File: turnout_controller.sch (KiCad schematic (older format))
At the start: 25 parts, among them J1 DCC Input, J2 Conn_01x04, J3 Servo Motor, J4 LED Connect, SW1 SW_Push, SW2 SW_Push, U1 AP65111A, U2 MKE04P24M48SF0

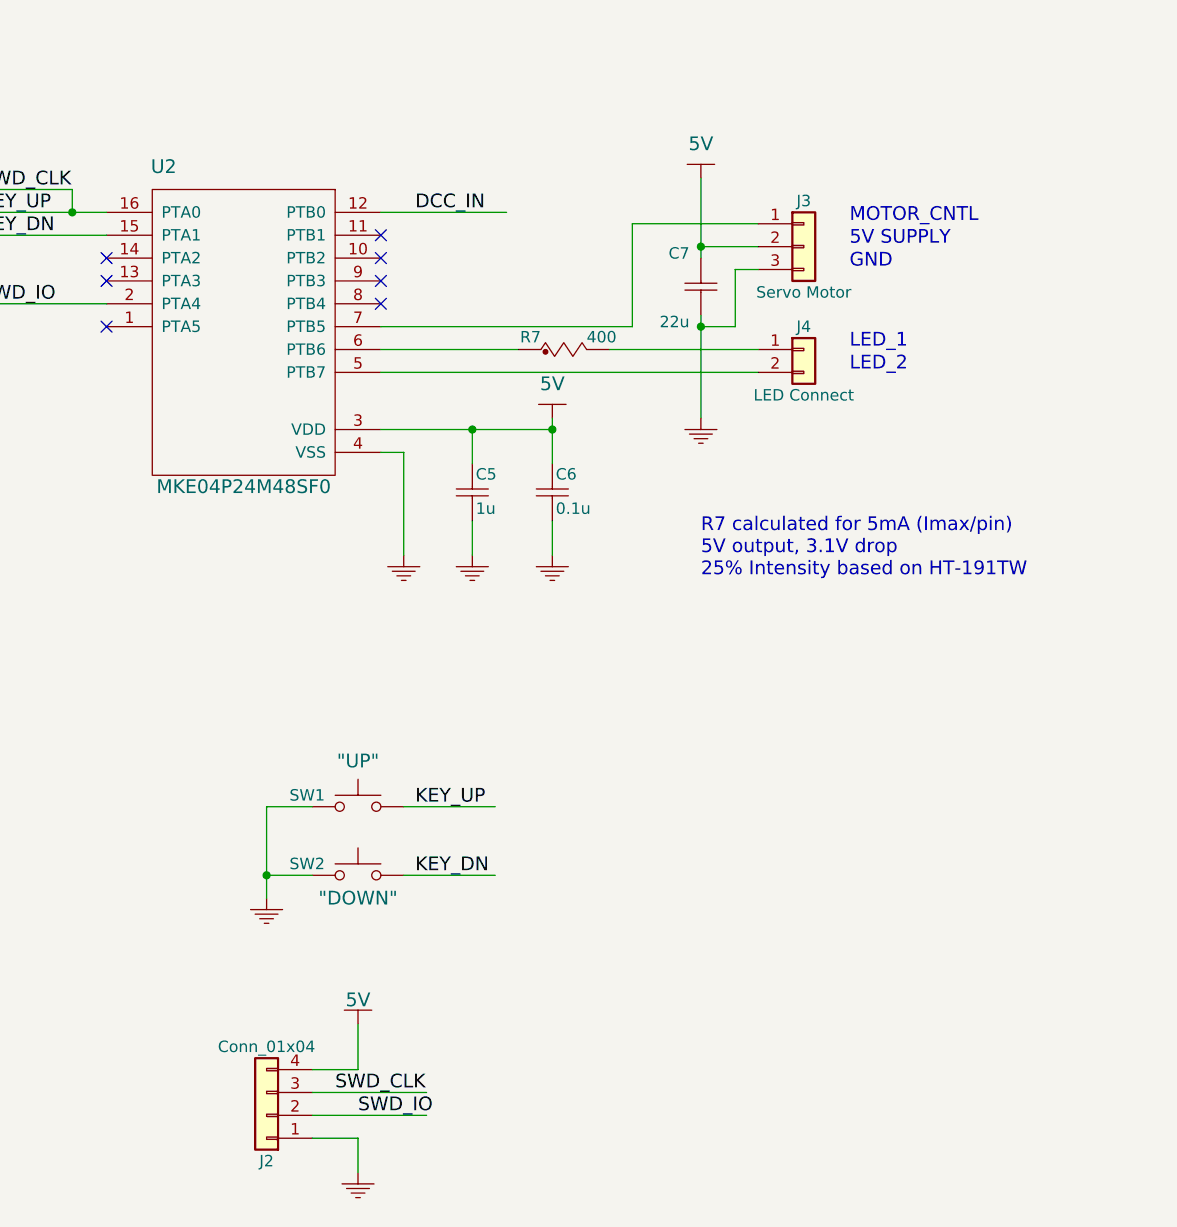
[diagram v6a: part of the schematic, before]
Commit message: 1. New PCB layout based around new positioning of buttons.
2. Optimizing distance between buck circuit components.

3. Added optional on-board LEDs.
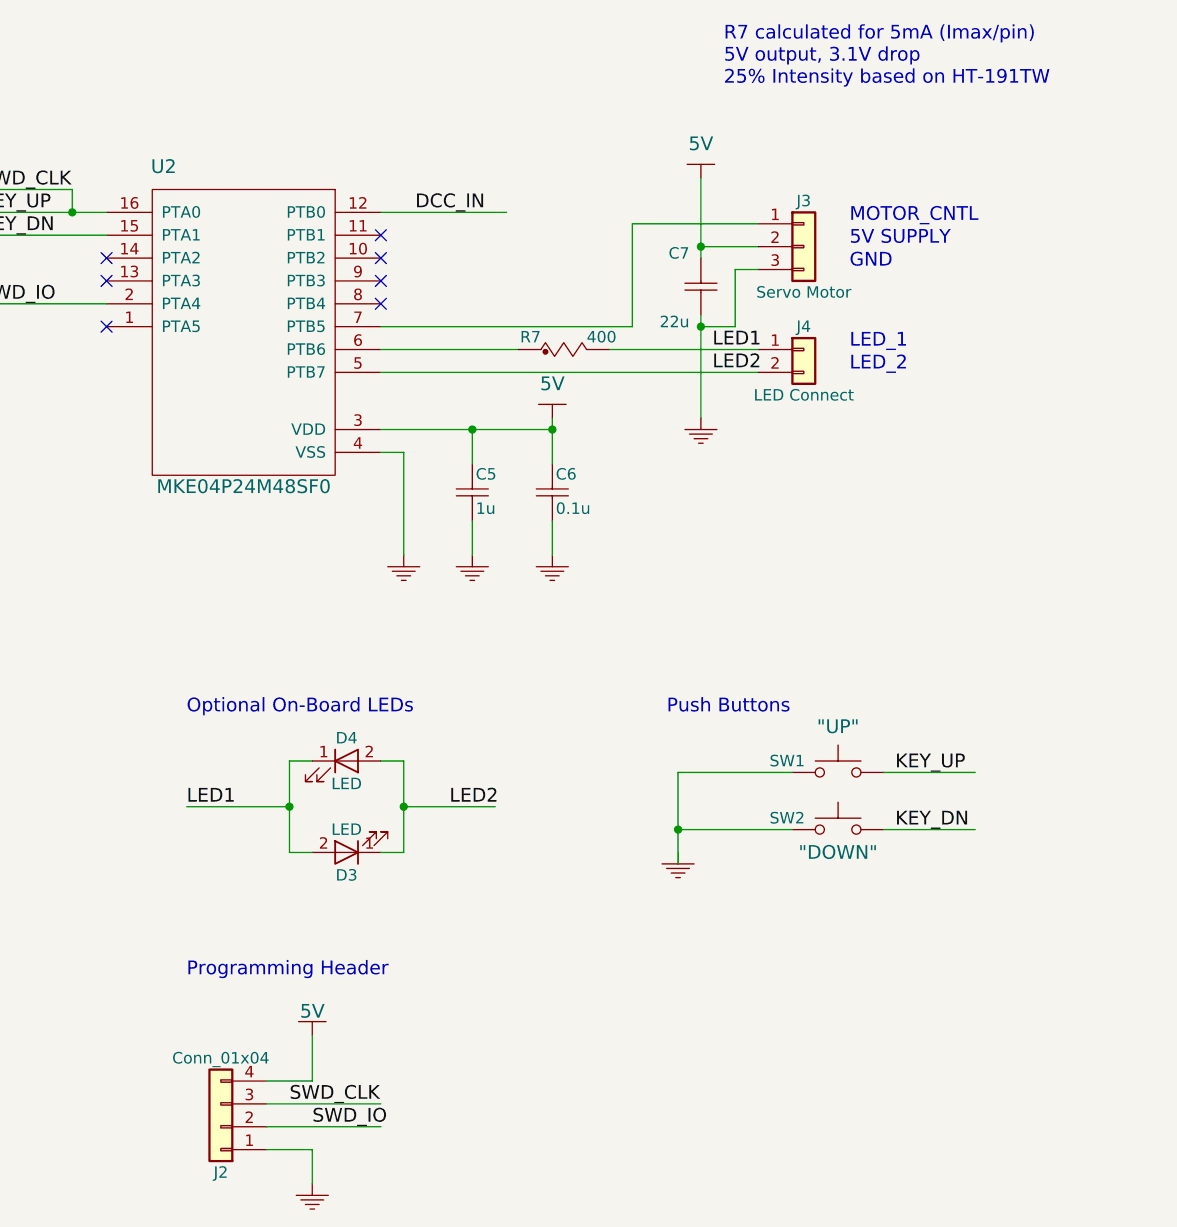
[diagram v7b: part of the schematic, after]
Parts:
- added D3, D4: LED, LEDs:LED_0603, symbol LED
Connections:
- net labels added: LED1, LED2
- wire segments 77 -> 85
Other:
- note added: "Optional On-Board LEDs"
- note added: "Programming Header"
- note added: "Push Buttons"
- moved on the sheet: J2, SW1, SW2
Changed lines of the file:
@@
 L SW_Push SW1
 U 1 1 5A1B3D6F
-P 7850 4000
-F 0 "SW1" H 7550 4050 50  0000 L CNN
-F 1 "SW_Push" H 7650 3950 50  0001 C CNN
-F 2 "tt_buttons:HTB1-Button" H 7850 4200 50  0001 C CNN
-F 3 "" H 7850 4200 50  0001 C CNN
-F 4 "TS-1289VE-4" H 7850 4000 60  0001 C CNN "MFG P/N"
-F 5 "\"UP\"" H 7850 4200 60  0000 C CNN "Label"
-	1    7850 4000
+P 9950 3850
+F 0 "SW1" H 9650 3900 50  0000 L CNN
+F 1 "SW_Push" H 9750 3800 50  0001 C CNN
+F 2 "tt_buttons:HTB1-Button" H 9950 4050 50  0001 C CNN
+F 3 "" H 9950 4050 50  0001 C CNN
+F 4 "TS-1289VE-4" H 9950 3850 60  0001 C CNN "MFG P/N"
+F 5 "\"UP\"" H 9950 4050 60  0000 C CNN "Label"
+	1    9950 3850
 	1    0    0    -1
 $EndComp
@@
 Text Label 6200 1500 0    60   ~ 0
 KEY_DN
-Text Label 8100 4000 0    60   ~ 0
+Text Label 10200 3850 0    60   ~ 0
 KEY_UP
-Text Label 8100 4300 0    60   ~ 0
+Text Label 10200 4100 0    60   ~ 0
 KEY_DN
 $Comp
 L SW_Push SW2
 U 1 1 5A1C72E9
-P 7850 4300
-F 0 "SW2" H 7550 4350 50  0000 L CNN
-F 1 "SW_Push" H 7650 4250 50  0001 C CNN
-F 2 "tt_buttons:HTB1-Button" H 7850 4500 50  0001 C CNN
-F 3 "" H 7850 4500 50  0001 C CNN
-F 4 "ZJWin-Tech" H 7850 4300 60  0001 C CNN "MFG"
-F 5 "TS-1289VE-4" H 7850 4300 60  0001 C CNN "P/N"
-F 6 "\"DOWN\"" H 7850 4200 60  0000 C CNN "Label"
-	1    7850 4300
+P 9950 4100
+F 0 "SW2" H 9650 4150 50  0000 L CNN
+F 1 "SW_Push" H 9750 4050 50  0001 C CNN
+F 2 "tt_buttons:HTB1-Button" H 9950 4300 50  0001 C CNN
+F 3 "" H 9950 4300 50  0001 C CNN
+F 4 "ZJWin-Tech" H 9950 4100 60  0001 C CNN "MFG"
+F 5 "TS-1289VE-4" H 9950 4100 60  0001 C CNN "P/N"
+F 6 "\"DOWN\"" H 9950 4000 60  0000 C CNN "Label"
+	1    9950 4100
 	1    0    0    -1
 $EndComp
@@
 L GND_ #PWR018
 U 1 1 5A1C74FD
-P 7450 4450
-F 0 "#PWR018" H 7550 4550 30  0001 C CNN
-F 1 "GND_" H 7450 4350 30  0001 C CNN
-F 2 "" H 7450 4450 60  0000 C CNN
-F 3 "" H 7450 4450 60  0000 C CNN
-	1    7450 4450
+P 9250 4250
+F 0 "#PWR018" H 9350 4350 30  0001 C CNN
+F 1 "GND_" H 9250 4150 30  0001 C CNN
+F 2 "" H 9250 4250 60  0000 C CNN
+F 3 "" H 9250 4250 60  0000 C CNN
+	1    9250 4250
 	1    0    0    -1
 $EndComp
@@
 $EndComp
 NoConn ~ 7950 1500
-Text Notes 9350 3000 0    60   ~ 0
+Text Notes 9450 850  0    60   ~ 0
 R7 calculated for 5mA (Imax/pin)\n5V output, 3.1V drop\n25% Intensity based on HT-191TW\n
 $Comp
@@
 	7950 2000 8550 2000
 Wire Wire Line
-	7950 2100 9600 2100
-Wire Wire Line
 	7950 1900 9050 1900
 Wire Wire Line
@@
 	6200 1400 6750 1400
 Wire Wire Line
-	8050 4300 8450 4300
-Wire Wire Line
-	8450 4000 8050 4000
-Wire Wire Line
-	7650 4000 7450 4000
-Wire Wire Line
-	7450 4000 7450 4400
-Wire Wire Line
-	7650 4300 7450 4300
-Connection ~ 7450 4300
+	10150 4100 10550 4100
+Wire Wire Line
+	10550 3850 10150 3850
+Wire Wire Line
+	9250 3850 9750 3850
+Wire Wire Line
+	9250 3850 9250 4250
+Wire Wire Line
+	9250 4100 9750 4100
+Connection ~ 9250 4100
 Wire Wire Line
 	2950 1250 2950 1350
@@
 	6750 1800 6200 1800
 Wire Wire Line
-	7650 5250 8150 5250
-Wire Wire Line
-	7650 5350 8150 5350
-Text Label 7850 5350 0    60   ~ 0
+	7450 5300 7950 5300
+Wire Wire Line
+	7450 5400 7950 5400
+Text Label 7650 5400 0    60   ~ 0
 SWD_IO
-Text Label 7750 5250 0    60   ~ 0
+Text Label 7550 5300 0    60   ~ 0
 SWD_CLK
 $Comp
 L Conn_01x04 J2
 U 1 1 5A77F62D
-P 7450 5350
-F 0 "J2" H 7450 5550 50  0000 C CNN
-F 1 "Conn_01x04" H 7450 5050 50  0000 C CNN
-F 2 "Socket_Strips:Socket_Strip_Straight_1x04_Pitch1.27mm" H 7450 5350 50  0001 C CNN
-F 3 "" H 7450 5350 50  0001 C CNN
-	1    7450 5350
+P 7250 5400
+F 0 "J2" H 7250 5600 50  0000 C CNN
+F 1 "Conn_01x04" H 7250 5100 50  0000 C CNN
+F 2 "Socket_Strips:Socket_Strip_Straight_1x04_Pitch1.27mm" H 7250 5400 50  0001 C CNN
+F 3 "" H 7250 5400 50  0001 C CNN
+	1    7250 5400
 	-1   0    0    1
 $EndComp
 Wire Wire Line
-	7650 5150 7850 5150
-Wire Wire Line
-	7850 5150 7850 4950
-Wire Wire Line
-	7650 5450 7850 5450
-Wire Wire Line
-	7850 5450 7850 5600
+	7450 5200 7650 5200
+Wire Wire Line
+	7650 5200 7650 5000
+Wire Wire Line
+	7450 5500 7650 5500
+Wire Wire Line
+	7650 5500 7650 5650
 $Comp
 L GND_ #PWR021
 U 1 1 5A77F939
-P 7850 5650
-F 0 "#PWR021" H 7950 5750 30  0001 C CNN
-F 1 "GND_" H 7850 5550 30  0001 C CNN
-F 2 "" H 7850 5650 60  0000 C CNN
-F 3 "" H 7850 5650 60  0000 C CNN
-	1    7850 5650
+P 7650 5700
+F 0 "#PWR021" H 7750 5800 30  0001 C CNN
+F 1 "GND_" H 7650 5600 30  0001 C CNN
+F 2 "" H 7650 5700 60  0000 C CNN
+F 3 "" H 7650 5700 60  0000 C CNN
+	1    7650 5700
 	1    0    0    -1
 $EndComp
@@
 L 5V #PWR022
 U 1 1 5A77FAA2
-P 7850 4950
-F 0 "#PWR022" H 7850 5050 40  0001 C CNN
-F 1 "5V" H 7850 5055 60  0000 C CNN
-F 2 "" H 7850 4950 60  0000 C CNN
-F 3 "" H 7850 4950 60  0000 C CNN
-	1    7850 4950
-	1    0    0    -1
-$EndComp
+P 7650 5000
+F 0 "#PWR022" H 7650 5100 40  0001 C CNN
+F 1 "5V" H 7650 5105 60  0000 C CNN
+F 2 "" H 7650 5000 60  0000 C CNN
+F 3 "" H 7650 5000 60  0000 C CNN
+	1    7650 5000
+	1    0    0    -1
+$EndComp
+$Comp
+L LED D3
+U 1 1 5AA49FFB
+P 7800 4200
+F 0 "D3" H 7800 4300 50  0000 C CNN
+F 1 "LED" H 7800 4100 50  0000 C CNN
+F 2 "LEDs:LED_0603" H 7800 4200 50  0001 C CNN
+F 3 "" H 7800 4200 50  0001 C CNN
+	1    7800 4200
+	-1   0    0    1
+$EndComp
+$Comp
+L LED D4
+U 1 1 5AA4A06E
+P 7800 3800
+F 0 "D4" H 7800 3900 50  0000 C CNN
+F 1 "LED" H 7800 3700 50  0000 C CNN
+F 2 "LEDs:LED_0603" H 7800 3800 50  0001 C CNN
+F 3 "" H 7800 3800 50  0001 C CNN
+	1    7800 3800
+	1    0    0    -1
+$EndComp
+Wire Wire Line
+	7550 4200 7650 4200
+Wire Wire Line
+	7550 3800 7550 4200
+Wire Wire Line
+	7550 3800 7650 3800
+Wire Wire Line
+	8050 4200 7950 4200
+Wire Wire Line
+	8050 3800 8050 4200
+Wire Wire Line
+	8050 3800 7950 3800
+Connection ~ 7550 4000
+Connection ~ 8050 4000
+Wire Wire Line
+	7950 2100 9600 2100
+Wire Wire Line
+	7100 4000 7550 4000
+Wire Wire Line
+	8050 4000 8450 4000
+Text Notes 7100 3600 0    60   ~ 0
+Optional On-Board LEDs
+Text Label 9400 2000 0    60   ~ 0
+LED1
+Text Label 9400 2100 0    60   ~ 0
+LED2
+Text Label 7100 4000 0    60   ~ 0
+LED1
+Text Label 8250 4000 0    60   ~ 0
+LED2
+Text Notes 9200 3600 0    60   ~ 0
+Push Buttons
+Text Notes 7100 4750 0    60   ~ 0
+Programming Header
 $EndSCHEMATC

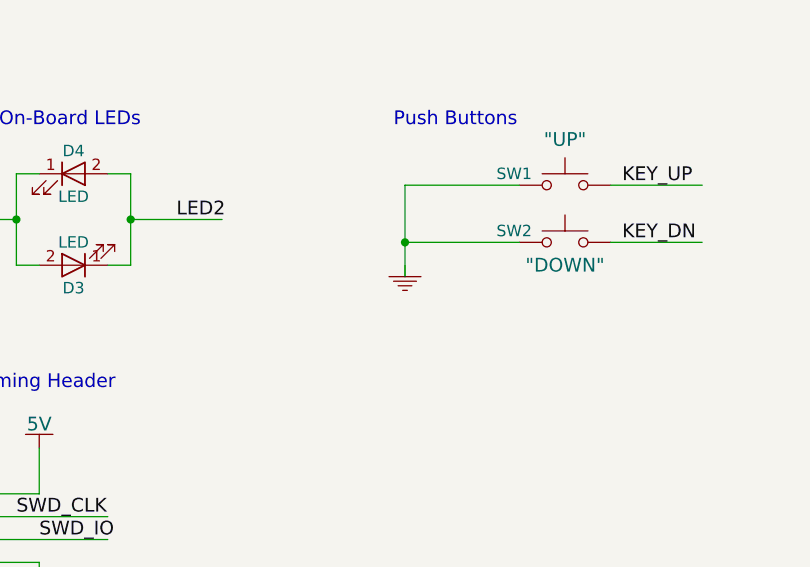
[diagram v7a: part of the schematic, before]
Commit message: updated PCB layout
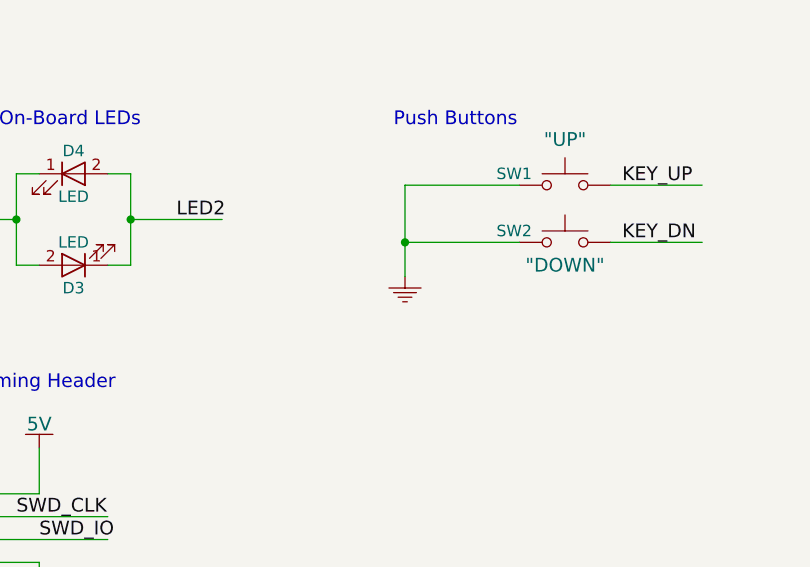
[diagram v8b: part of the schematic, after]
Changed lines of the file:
@@
 LIBS:contrib
 LIBS:valves
-LIBS:teletram
-LIBS:tt-power
 LIBS:turnout_controller-cache
 EELAYER 25 0
@@
 L GND_ #PWR018
 U 1 1 5A1C74FD
-P 9250 4250
-F 0 "#PWR018" H 9350 4350 30  0001 C CNN
-F 1 "GND_" H 9250 4150 30  0001 C CNN
-F 2 "" H 9250 4250 60  0000 C CNN
-F 3 "" H 9250 4250 60  0000 C CNN
-	1    9250 4250
-	1    0    0    -1
-$EndComp
+P 9250 4300
+F 0 "#PWR018" H 9350 4400 30  0001 C CNN
+F 1 "GND_" H 9250 4200 30  0001 C CNN
+F 2 "" H 9250 4300 60  0000 C CNN
+F 3 "" H 9250 4300 60  0000 C CNN
+	1    9250 4300
+	1    0    0    -1
+$EndComp
